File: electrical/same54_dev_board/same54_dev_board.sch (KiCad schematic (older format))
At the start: 2 parts

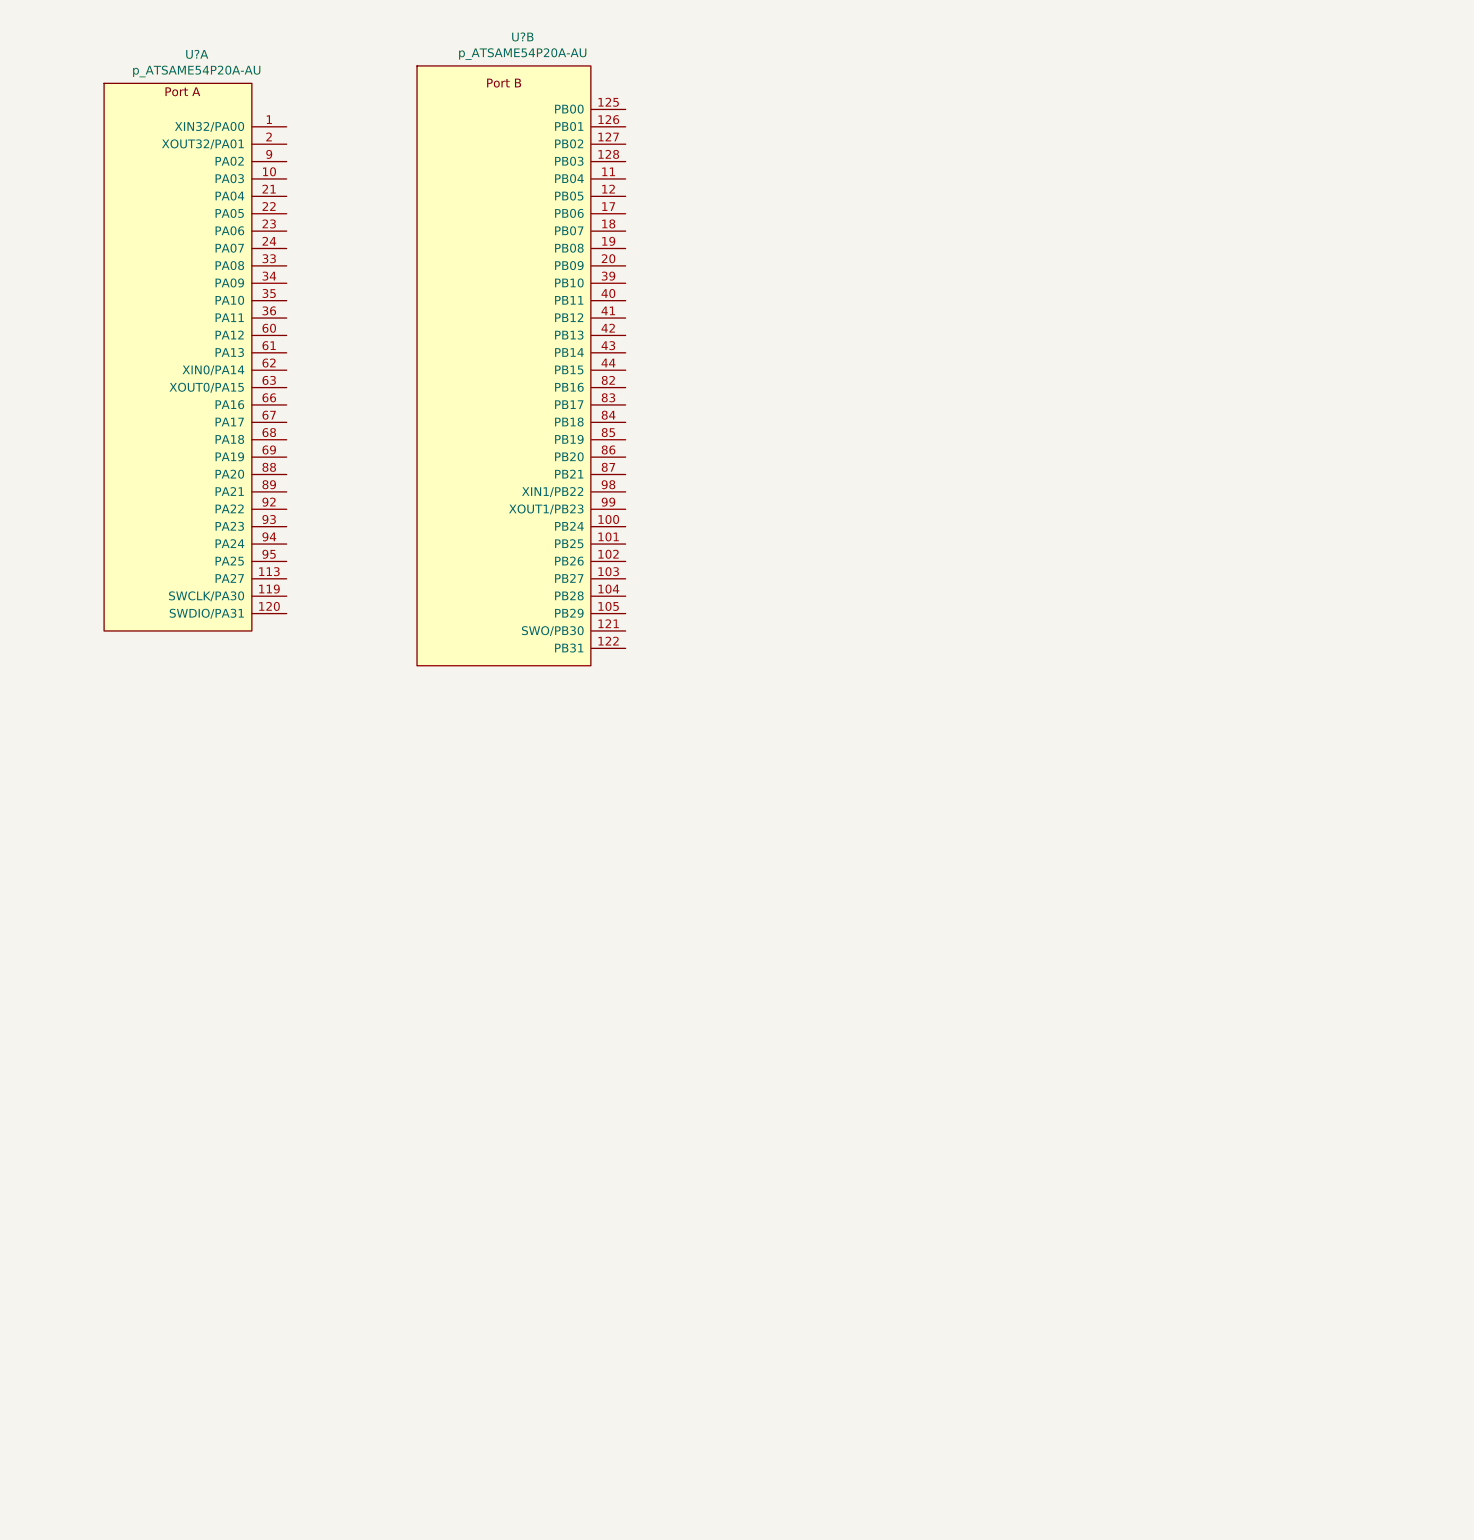
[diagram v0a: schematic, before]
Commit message: finished same54 symbol, added some more symbols, created 2x20 connector for lcd
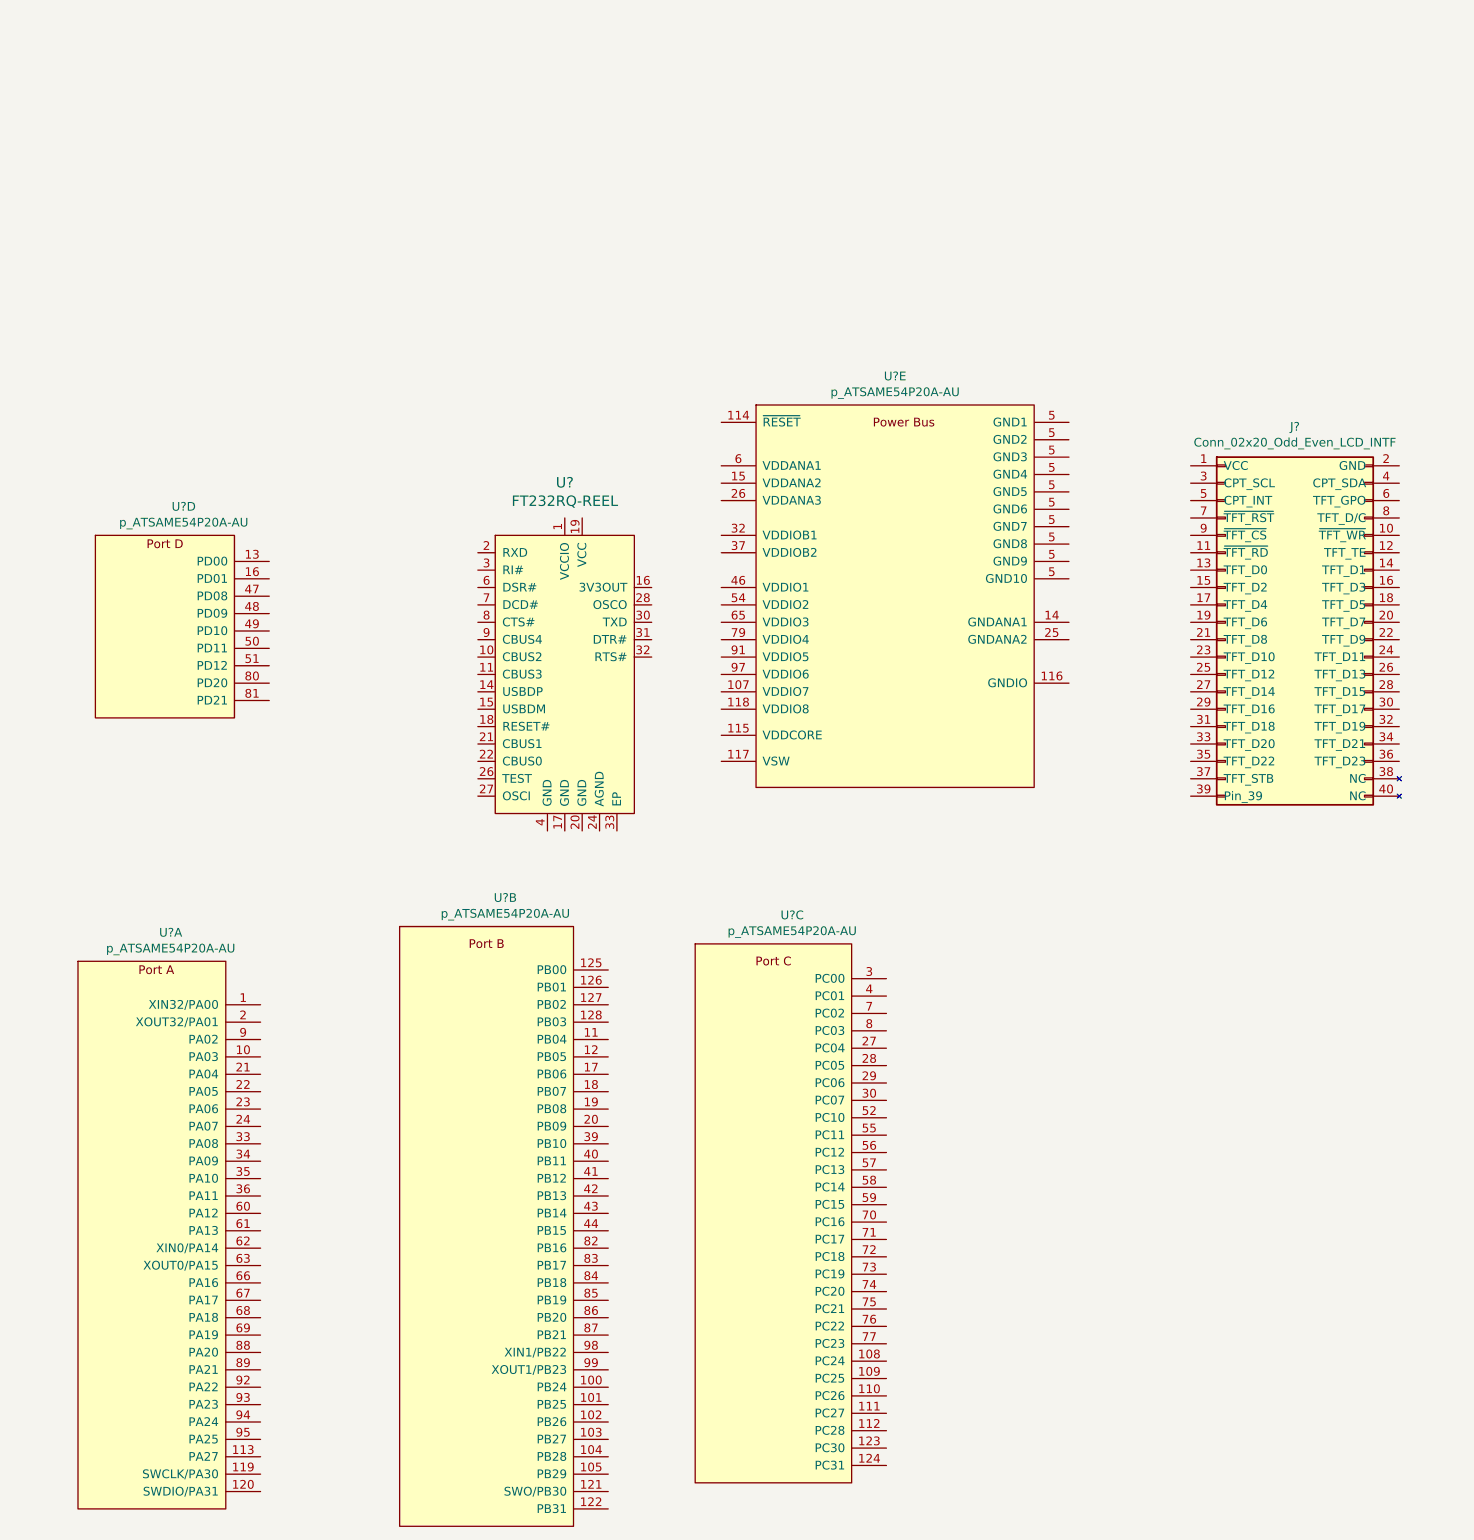
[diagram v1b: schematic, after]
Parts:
- removed U? (x2): p_ATSAME54P20A-AU, symbol p_ATSAME54P20A-AU:p_ATSAME54P20A-AU
- added J?: Conn_02x20_Odd_Even_LCD_INTF, symbol Conn_02x20_LCD_INTF:Conn_02x20_Odd_Even_LCD_INTF
- added U?: FT232RQ-REEL, digikey-footprints:QFN-32-1EP_5x5mm, symbol dk_Interface-Controllers:FT232RQ-REEL
- added U? (x5): p_ATSAME54P20A-AU, symbol p_ATSAME54P20A-AU:p_ATSAME54P20A-AU
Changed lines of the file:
@@
 EELAYER 30 0
 EELAYER END
-$Descr A4 11693 8268
+$Descr USLedger 17000 11000
 encoding utf-8
 Sheet 1 1
-Title ""
-Date ""
-Rev ""
+Title "Project Oracle"
+Date "2020-03-16"
+Rev "v0.1"
 Comp ""
 Comment1 ""
@@
 $EndDescr
 $Comp
-L p_ATSAME54P20A-AU:p_ATSAME54P20A-AU U?
-U 1 1 5E73E542
-P 1500 2100
-F 0 "U?" H 1583 3265 50  0000 C CNN
-F 1 "p_ATSAME54P20A-AU" H 1583 3174 50  0000 C CNN
-F 2 "" H 300 3350 50  0001 C CNN
-F 3 "" H 300 3350 50  0001 C CNN
-	1    1500 2100
+L dk_Interface-Controllers:FT232RQ-REEL U?
+U 1 1 5E77AB6E
+P 3900 3700
+F 0 "U?" H 3700 4003 60  0000 C CNN
+F 1 "FT232RQ-REEL" H 3700 3897 60  0000 C CNN
+F 2 "digikey-footprints:QFN-32-1EP_5x5mm" H 4100 3900 60  0001 L CNN
+F 3 "https://www.ftdichip.com/Support/Documents/DataSheets/ICs/DS_FT232R.pdf" H 4100 4000 60  0001 L CNN
+F 4 "768-1008-1-ND" H 4100 4100 60  0001 L CNN "Digi-Key_PN"
+F 5 "FT232RQ-REEL" H 4100 4200 60  0001 L CNN "MPN"
+F 6 "Integrated Circuits (ICs)" H 4100 4300 60  0001 L CNN "Category"
+F 7 "Interface - Controllers" H 4100 4400 60  0001 L CNN "Family"
+F 8 "https://www.ftdichip.com/Support/Documents/DataSheets/ICs/DS_FT232R.pdf" H 4100 4500 60  0001 L CNN "DK_Datasheet_Link"
+F 9 "/product-detail/en/ftdi-future-technology-devices-international-ltd/FT232RQ-REEL/768-1008-1-ND/1836403" H 4100 4600 60  0001 L CNN "DK_Detail_Page"
+F 10 "IC USB FS SERIAL UART 32-QFN" H 4100 4700 60  0001 L CNN "Description"
+F 11 "FTDI, Future Technology Devices International Ltd" H 4100 4800 60  0001 L CNN "Manufacturer"
+F 12 "Active" H 4100 4900 60  0001 L CNN "Status"
+	1    3900 3700
 	1    0    0    -1
 $EndComp
 $Comp
 L p_ATSAME54P20A-AU:p_ATSAME54P20A-AU U?
-U 2 1 5E742312
-P 3350 1900
-F 0 "U?" H 3458 2965 50  0000 C CNN
-F 1 "p_ATSAME54P20A-AU" H 3458 2874 50  0000 C CNN
-F 2 "" H 2150 3150 50  0001 C CNN
-F 3 "" H 2150 3150 50  0001 C CNN
-	2    3350 1900
+U 1 1 5E7D4D4E
+P 1350 7150
+F 0 "U?" H 1433 8315 50  0000 C CNN
+F 1 "p_ATSAME54P20A-AU" H 1433 8224 50  0000 C CNN
+F 2 "" H 150 8400 50  0001 C CNN
+F 3 "" H 150 8400 50  0001 C CNN
+	1    1350 7150
 	1    0    0    -1
 $EndComp
+$Comp
+L p_ATSAME54P20A-AU:p_ATSAME54P20A-AU U?
+U 2 1 5E7D76F8
+P 3250 6850
+F 0 "U?" H 3358 7915 50  0000 C CNN
+F 1 "p_ATSAME54P20A-AU" H 3358 7824 50  0000 C CNN
+F 2 "" H 2050 8100 50  0001 C CNN
+F 3 "" H 2050 8100 50  0001 C CNN
+	2    3250 6850
+	1    0    0    -1
+$EndComp
+$Comp
+L p_ATSAME54P20A-AU:p_ATSAME54P20A-AU U?
+U 3 1 5E7DA3E5
+P 4900 6900
+F 0 "U?" H 5008 7915 50  0000 C CNN
+F 1 "p_ATSAME54P20A-AU" H 5008 7824 50  0000 C CNN
+F 2 "" H 3700 8150 50  0001 C CNN
+F 3 "" H 3700 8150 50  0001 C CNN
+	3    4900 6900
+	1    0    0    -1
+$EndComp
+$Comp
+L p_ATSAME54P20A-AU:p_ATSAME54P20A-AU U?
+U 4 1 5E7DD1DD
+P 1400 4600
+F 0 "U?" H 1508 5665 50  0000 C CNN
+F 1 "p_ATSAME54P20A-AU" H 1508 5574 50  0000 C CNN
+F 2 "" H 200 5850 50  0001 C CNN
+F 3 "" H 200 5850 50  0001 C CNN
+	4    1400 4600
+	1    0    0    -1
+$EndComp
+$Comp
+L p_ATSAME54P20A-AU:p_ATSAME54P20A-AU U?
+U 5 1 5E7E22D4
+P 5600 3700
+F 0 "U?" H 5600 4615 50  0000 C CNN
+F 1 "p_ATSAME54P20A-AU" H 5600 4524 50  0000 C CNN
+F 2 "" H 4400 4950 50  0001 C CNN
+F 3 "" H 4400 4950 50  0001 C CNN
+	5    5600 3700
+	1    0    0    -1
+$EndComp
+$Comp
+L Conn_02x20_LCD_INTF:Conn_02x20_Odd_Even_LCD_INTF J?
+U 1 1 5E896181
+P 7900 4200
+F 0 "J?" H 7900 5325 50  0000 C CNN
+F 1 "Conn_02x20_Odd_Even_LCD_INTF" H 7900 5234 50  0000 C CNN
+F 2 "" H 7500 4200 50  0001 C CNN
+F 3 "~" H 7500 4200 50  0001 C CNN
+	1    7900 4200
+	1    0    0    -1
+$EndComp

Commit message: made some connections, creating firmware base from asf4
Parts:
- added U?: MAX7301AAX+, SOP80P1030X264-36N, symbol MAX7301AAX_:MAX7301AAX+
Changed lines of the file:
@@
+	1    0    0    -1
+$EndComp
+$Comp
+L MAX7301AAX_:MAX7301AAX+ U?
+U 1 1 5E8C31CA
+P 7000 7450
+F 0 "U?" H 7000 8920 50  0000 C CNN
+F 1 "MAX7301AAX+" H 7000 8829 50  0000 C CNN
+F 2 "SOP80P1030X264-36N" H 7000 7450 50  0001 L BNN
+F 3 "Maxim Integrated" H 7000 7450 50  0001 L BNN
+F 4 "None" H 7000 7450 50  0001 L BNN "Field4"
+F 5 "Interface IC - I/O extensions Maxim Integrated MAX7301AAX+ SPI 26 MHz SSOP 36" H 7000 7450 50  0001 L BNN "Field5"
+F 6 "SSOP-36 Maxim" H 7000 7450 50  0001 L BNN "Field6"
+F 7 "Unavailable" H 7000 7450 50  0001 L BNN "Field7"
+F 8 "MAX7301AAX+" H 7000 7450 50  0001 L BNN "Field8"
+	1    7000 7450
 	1    0    0    -1
 $EndComp
